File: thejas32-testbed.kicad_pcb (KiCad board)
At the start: 4 copper layers, 141.5 x 110 mm, 102 parts, among them J1 Conn_02x04_Odd_Even, J10 Conn_02x10_Odd_Even, J11 Conn_02x03_Odd_Even, J12 Conn_02x20_Odd_Even, J13 Conn_02x06_Odd_Even, J2 USB_B_Micro, J3 Conn_02x03_Odd_Even, J4 Conn_02x04_Odd_Even, J6 Conn_02x06_Odd_Even, J7 Conn_01x06, U1 Pico Master, U2 THEJAS32, U3 Pico Slave, U6 W25Q16JVSSIQ

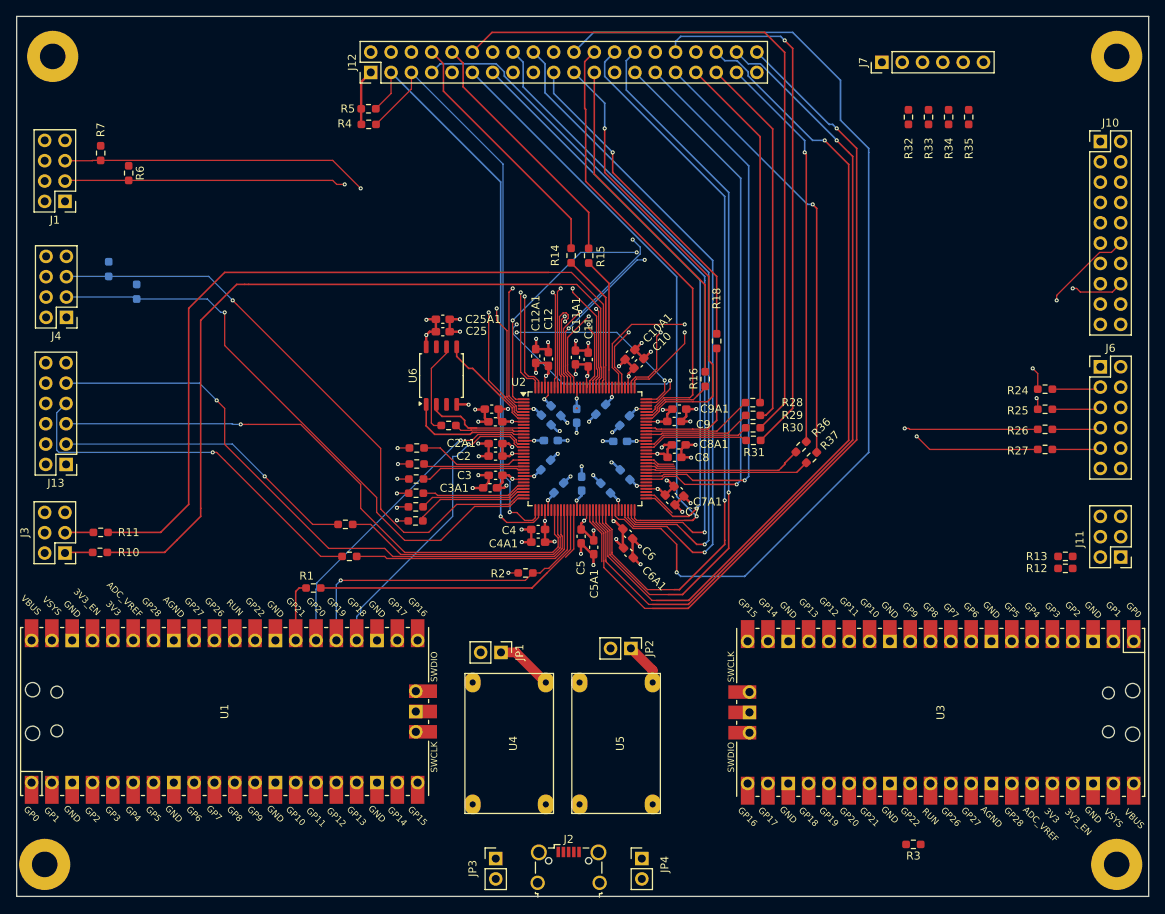
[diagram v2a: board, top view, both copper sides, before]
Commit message: Review,power shapes,dcap placement from Atharva
All dcaps are now at layer 4, leaving lot
more space on layer 1 for signal breakout.

Flow of 1V2 power is deemed good - power plane,
flowing to caps, through via to pins. Flow of 3V3
power is reasonable - power plane with vias to both
caps and pins.

Connectors and component placements need to be
finalized next, and routed.
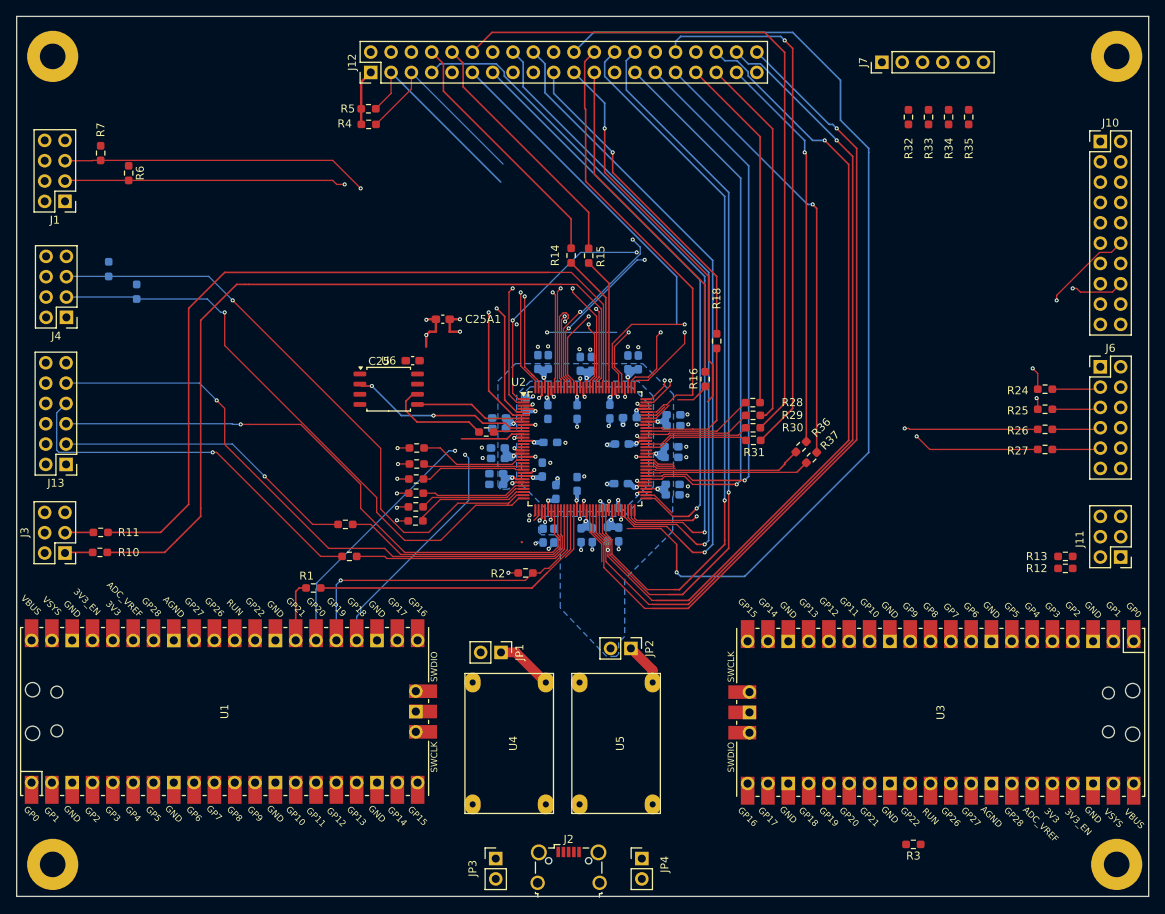
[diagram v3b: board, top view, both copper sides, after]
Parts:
- C1, C10, C10A1, C11, C11A1, C12, C12A1, C1A1, C2, C2A1, C3, C3A1, C4, C4A1, C5, C5A1, C6, C6A1, C7, C7A1, C8, C8A1, C9, C9A1: moved to B.Cu
- moved U6 6.81 mm to (131.0, 96.6), turned to 0 degrees
- moved C25 5.22 mm to (134.0, 93.0), turned to 180 degrees
- moved R70 4.78 mm to (143.2, 102.0)
- moved C13 3.13 mm to (148.2, 98.5), turned to 90 degrees
- moved C6A1 2.60 mm to (159.8, 114.8), turned to -90 degrees
- moved C1A1 2.58 mm to (144.8, 101.5)
- moved C18 2.55 mm to (158.8, 111.4), turned to 180 degrees
- moved C6 2.53 mm to (158.3, 114.7), turned to -90 degrees
- moved C5A1 2.19 mm to (155.1, 114.8)
- moved C4A1 2.12 mm to (151.7, 114.9), turned to -90 degrees
- moved C2A1 1.88 mm to (144.7, 105.2)
- moved C12A1 1.74 mm to (150.9, 93.2)
- moved C10A1 1.44 mm to (162.2, 93.2), turned to 90 degrees
- moved C5 1.40 mm to (156.4, 114.8)
- moved C10 1.38 mm to (160.9, 93.2), turned to 90 degrees
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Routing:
- net RPi_COMPAT_I2C1_SCL: track 73.2 -> 25.4 mm
- net RPi_COMPAT_I2C1_SDA: track 72.7 -> 26.2 mm
- net RPi_COMPAT_GPIO_17: track 76.2 -> 51.2 mm
- net Net-(J1-Pin_5): track 93.7 -> 69.7 mm
- net PWR_3V3: track 65.0 -> 41.1 mm
- net GND: track 83.1 -> 60.1 mm, vias 46 -> 65
- net PWR_1V2: track 81.6 -> 60.9 mm, vias 24 -> 12
- net Net-(J1-Pin_3): track 91.2 -> 80.5 mm
- net MCU_BOOT_SEL: track 41.5 -> 31.4 mm
- net MCU_HEART_BEAT: track 38.6 -> 29.2 mm
- net Net-(U2-SPI3_MISO): track 13.8 -> 22.7 mm, vias 0 -> 2
- net Net-(U2-SPI3_SS): track 15.5 -> 8.03 mm
- net RPi_COMPAT_SPI0_MISO: track 57.3 -> 52.2 mm
- net Net-(U2-SPI3_SCLK): track 8.80 -> 3.80 mm
- net RPi_COMPAT_GPIO_25: track 128.8 -> 125.9 mm
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- added copper zone on B.Cu, net GND
- added copper zone on In1.Cu, net GND
- added copper zone on B.Cu, net PWR_1V2
- removed copper zone on In2.Cu, net PWR_1V2

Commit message: Remap pins for less criss cross. Get rid of tracks
Got rid of tracks to start tracks afresh once placement is
done.
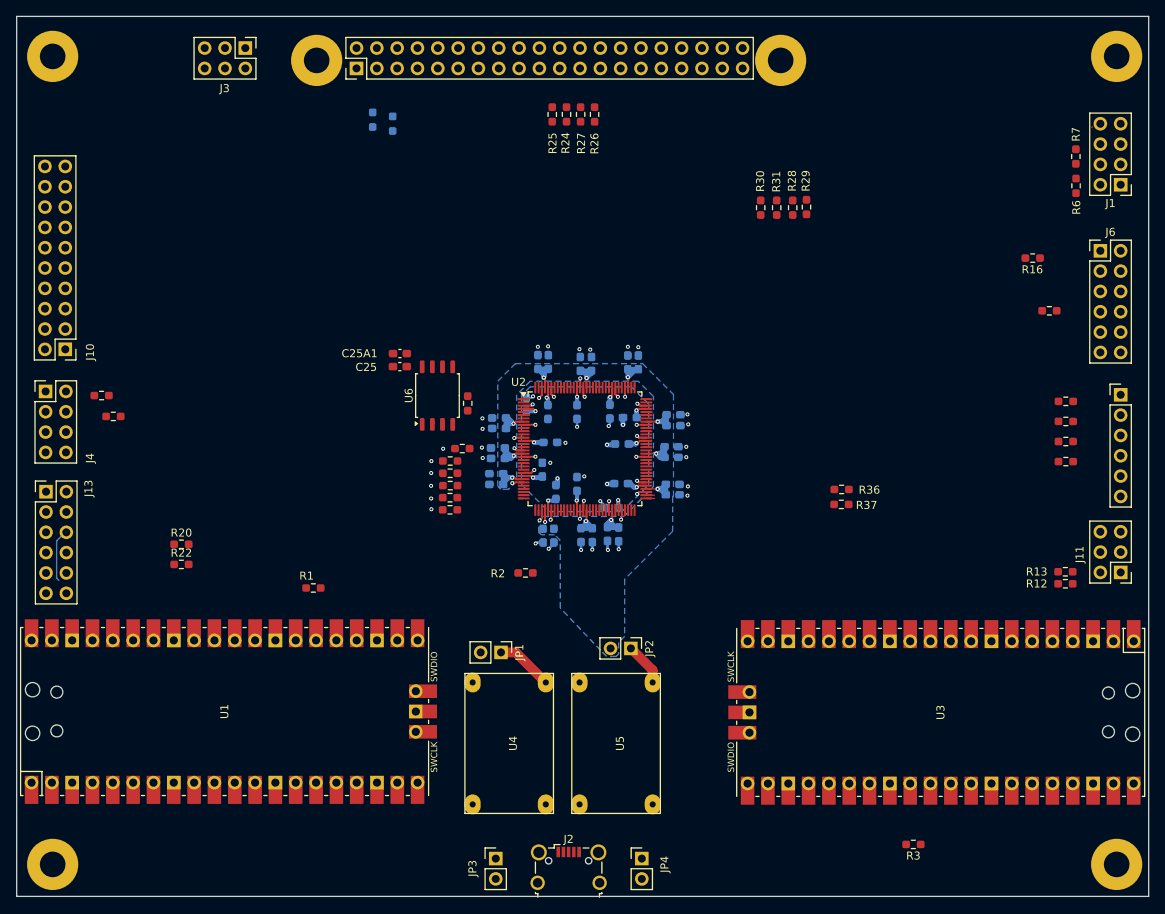
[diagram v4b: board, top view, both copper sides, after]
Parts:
- removed R10, R11, R14, R15: 0E, project_lib:proj_R_0603_1608Metric_Pad0.98x0.95mm_HandSolder
- added TP5: Mounting Hole, MountingHole:MountingHole_3.2mm_M3_Pad, F.Cu at (122.0, 55.5)
- added TP6: Mounting Hole, MountingHole:MountingHole_3.2mm_M3_Pad, F.Cu at (180.0, 55.5)
- moved J1 132.0 mm to (222.5, 71.0)
- moved J10 132.0 mm to (90.6, 91.6), turned to 180 degrees
- moved R7 121.9 mm to (216.9, 67.5), turned to 90 degrees
- moved R6 118.4 mm to (216.9, 71.2), turned to 90 degrees
- moved R25 71.8 mm to (151.4, 62.3), turned to 90 degrees
- moved R27 71.6 mm to (155.0, 62.3), turned to 90 degrees
- moved R24 69.0 mm to (153.2, 62.3), turned to 90 degrees
- moved R26 68.7 mm to (156.7, 62.3), turned to 90 degrees
- moved J3 67.0 mm to (113.1, 54.0), turned to -90 degrees
- moved J7 51.2 mm to (222.5, 97.3), turned to 0 degrees
- moved R5 50.0 mm to (96.6, 100.0), turned to 180 degrees
- moved R4 47.6 mm to (95.1, 97.4), turned to 180 degrees
- moved R35 44.7 mm to (215.6, 105.7), turned to 0 degrees
- moved R16 43.6 mm to (211.5, 80.2), turned to 180 degrees
- moved R34 43.1 mm to (215.6, 103.1), turned to 0 degrees
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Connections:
- net MCU_SPI2_CSN renamed MCU_SPI0_CSN
- net MCU_SPI2_MISO renamed MCU_SPI0_MISO
- net MCU_SPI2_MOSI renamed MCU_SPI0_MOSI
- net MCU_SPI2_SCK renamed MCU_SPI0_SCK
- J10 pad 10: MCU_GPIO_27 -> MCU_GPIO_22
- J10 pad 11: MCU_GPIO_20 -> MCU_GPIO_25
- J10 pad 12: MCU_GPIO_28 -> MCU_GPIO_24
- J10 pad 13: MCU_GPIO_21 -> MCU_GPIO_27
- J10 pad 14: MCU_GPIO_29 -> MCU_GPIO_26
- J10 pad 15: MCU_GPIO_22 -> MCU_GPIO_29
- J10 pad 16: MCU_GPIO_30 -> MCU_GPIO_28
- J10 pad 17: MCU_GPIO_23 -> MCU_GPIO_31
- J10 pad 18: MCU_GPIO_31 -> MCU_GPIO_30
- J10 pad 3: MCU_GPIO_16 -> MCU_GPIO_17
- J10 pad 4: MCU_GPIO_24 -> MCU_GPIO_16
- J10 pad 5: MCU_GPIO_17 -> MCU_GPIO_19
- J10 pad 6: MCU_GPIO_25 -> MCU_GPIO_18
- J10 pad 7: MCU_GPIO_18 -> MCU_GPIO_21
- J10 pad 8: MCU_GPIO_26 -> MCU_GPIO_20
- J10 pad 9: MCU_GPIO_19 -> MCU_GPIO_23
- J4 pad 4: MCU_I2C2_SCL -> MCU_I2C0_SCL
- J4 pad 6: MCU_I2C2_SDA -> MCU_I2C0_SCL
- R16 pad 2: RPi_COMPAT_SPI0_SCLK -> Net-(J6-Pin_3)
- R18 pad 2: RPi_COMPAT_SPI0_MOSI -> Net-(J6-Pin_7)
- R24 pad 2: Net-(J6-Pin_3) -> RPi_COMPAT_SPI0_SCLK
- R25 pad 2: Net-(J6-Pin_5) -> RPi_COMPAT_SPI0_CE0
- R26 pad 2: Net-(J6-Pin_7) -> RPi_COMPAT_SPI0_MOSI
- R27 pad 2: Net-(J6-Pin_9) -> RPi_COMPAT_SPI0_MISO
- R36 pad 2: RPi_COMPAT_GPIO_26 -> RPi_COMPAT_GPIO_4
- R37 pad 2: RPi_COMPAT_GPIO_6 -> RPi_COMPAT_GPIO_17
- R4 pad 2: RPi_COMPAT_I2C1_SCL -> Net-(J4-Pin_3)
- R5 pad 2: RPi_COMPAT_I2C1_SDA -> Net-(J4-Pin_5)
- R8 pad 2: Net-(J4-Pin_3) -> RPi_COMPAT_I2C1_SCL
- R9 pad 2: Net-(J4-Pin_5) -> RPi_COMPAT_I2C1_SDA
- U1 pad 10: MCU_I2C1_SDA -> MCU_I2C0_SCL
- U1 pad 9: MCU_I2C1_SCL -> MCU_I2C0_SCL
- U2 pad 105: Net-(U2-UART2_RX) -> RPi_COMPAT_UART_RXD
- U2 pad 106: Net-(U2-UART2_TX) -> RPi_COMPAT_UART_TXD
- U2 pad 107: Net-(U2-UART0_RX) -> Net-(J3-Pin_3)
- U2 pad 108: Net-(U2-UART0_TX) -> Net-(J3-Pin_1)
- U2 pad 31: Net-(J4-Pin_5) -> RPi_COMPAT_I2C1_SDA
- U2 pad 32: Net-(J4-Pin_3) -> RPi_COMPAT_I2C1_SCL
- U2 pad 33: RPi_COMPAT_I2C1_SCL -> Net-(J4-Pin_3)
- U2 pad 34: RPi_COMPAT_I2C1_SDA -> Net-(J4-Pin_5)
- U2 pad 53: RPi_COMPAT_GPIO_16 -> RPi_COMPAT_GPIO_26
- U2 pad 54: RPi_COMPAT_GPIO_1 -> RPi_COMPAT_GPIO_16
- U2 pad 55: RPi_COMPAT_GPIO_7 -> RPi_COMPAT_GPIO_6
- U2 pad 58: RPi_COMPAT_GPIO_25 -> RPi_COMPAT_GPIO_5
- U2 pad 61: RPi_COMPAT_GPIO_24 -> RPi_COMPAT_GPIO_0
- U2 pad 62: RPi_COMPAT_GPIO_23 -> RPi_COMPAT_GPIO_1
- U2 pad 63: RPi_COMPAT_GPIO_4 -> RPi_COMPAT_GPIO_7
- U2 pad 64: RPi_COMPAT_GPIO_17 -> RPi_COMPAT_GPIO_25
- U2 pad 65: RPi_COMPAT_GPIO_27 -> RPi_COMPAT_GPIO_24
- U2 pad 71: RPi_COMPAT_GPIO_0 -> RPi_COMPAT_GPIO_23
- U2 pad 72: RPi_COMPAT_GPIO_5 -> RPi_COMPAT_GPIO_27
- U2 pad 90: RPi_COMPAT_SPI0_MISO -> Net-(J6-Pin_9)
- U2 pad 92: RPi_COMPAT_SPI0_CE0 -> Net-(J6-Pin_5)
- U3 pad 10: MCU_I2C2_SDA -> MCU_I2C1_SDA
- U3 pad 9: MCU_I2C2_SCL -> MCU_I2C1_SCL
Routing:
- net RPi_COMPAT_GPIO_25: track 125.9 -> 0.00 mm, vias 1 -> 0
- net MCU_GPIO_24: track 109.6 -> 0.00 mm, vias 1 -> 0
- net RPi_COMPAT_GPIO_21: track 104.1 -> 0.00 mm, vias 1 -> 0
- net RPi_COMPAT_GPIO_16: track 104.0 -> 0.00 mm, vias 1 -> 0
- net RPi_COMPAT_GPIO_20: track 103.9 -> 0.00 mm, vias 1 -> 0
- net Net-(U2-UART0_RX): track 101.8 -> 0.00 mm
- net Net-(U2-UART0_TX): track 101.2 -> 0.00 mm
- net MCU_GPIO_16: track 100.9 -> 0.00 mm, vias 1 -> 0
- net MCU_GPIO_25: track 100.0 -> 0.00 mm, vias 1 -> 0
- net MCU_GPIO_17: track 97.9 -> 0.00 mm, vias 1 -> 0
- net MCU_GPIO_18: track 94.3 -> 0.00 mm, vias 1 -> 0
- net RPi_COMPAT_GPIO_1: track 93.1 -> 0.00 mm, vias 1 -> 0
- net MCU_GPIO_21: track 92.7 -> 0.00 mm, vias 1 -> 0
- net RPi_COMPAT_GPIO_7: track 92.4 -> 0.00 mm, vias 1 -> 0
- net MCU_GPIO_19: track 92.5 -> 0.62 mm, vias 2 -> 0
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
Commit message: Potentially cleaner routing
Main changes:

- No more than 1 via on high speed trace (e.g. SPI)
- Use two vias on slower GPIOs to maintain topology
- Use via on the thick 5V trace supplying power to
  RPi connector
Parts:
- removed R12, R13: 0E, project_lib:proj_R_0603_1608Metric_Pad0.98x0.95mm_HandSolder
- J7: value Conn_01x06 -> Conn_01x05; footprint Connector_PinHeader_2.54mm:PinHeader_1x06_P2.54mm_Vertical -> Connector_PinHeader_2.54mm:PinHeader_1x05_P2.54mm_Vertical
- R16, R18, R32, R33, R34, R35, R36, R37, R6, R7: moved to B.Cu
- R8: moved to F.Cu
- moved R35 43.4 mm to (175.0, 121.0)
- moved R28 20.6 mm to (161.1, 76.2)
- moved R29 20.5 mm to (162.9, 76.2)
- moved R31 13.2 mm to (166.5, 76.3)
- moved R30 13.0 mm to (164.7, 76.3)
- moved J6 13.0 mm to (222.5, 92.0), turned to 180 degrees
- moved R24 12.5 mm to (153.0, 74.8)
- moved R27 12.5 mm to (155.0, 74.8)
- moved R25 12.3 mm to (151.0, 74.6)
- moved R26 12.3 mm to (157.0, 74.6)
- moved R36 9.27 mm to (180.1, 103.7)
- moved R37 9.27 mm to (180.1, 105.6)
- moved R16 8.55 mm to (213.6, 88.5), turned to 0 degrees
- moved R20 7.57 mm to (97.6, 117.0), turned to 180 degrees
- moved R7 6.51 mm to (217.4, 74.0), turned to 0 degrees
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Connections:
- J4 pad 6: MCU_I2C0_SCL -> MCU_I2C0_SDA
- J7 pad 5: MCU_PWM_7 -> GND
- U1 pad 10: MCU_I2C0_SCL -> MCU_I2C0_SDA
- U1 pad 25: MCU_RESETN -> unconnected-(U1-GPIO19-Pad25)
- U2 pad 45: Net-(U2-UART1_TX) -> Net-(J11-Pin_1)
- U2 pad 50: Net-(U2-UART1_RX) -> Net-(J11-Pin_3)
- U2 pad 61: RPi_COMPAT_GPIO_0 -> RPi_COMPAT_GPIO_1
- U2 pad 62: RPi_COMPAT_GPIO_1 -> RPi_COMPAT_GPIO_0
- U2 pad 66: RPi_COMPAT_GPIO_22 -> RPi_COMPAT_GPIO_23
- U2 pad 71: RPi_COMPAT_GPIO_23 -> RPi_COMPAT_GPIO_22
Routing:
- net PWR_3V3: track 28.4 -> 467.2 mm, vias 12 -> 15
- net PICO_SLAVE_RUN: track 0.00 -> 136.8 mm
- net PICO_COMM_1: track 0.00 -> 99.4 mm
- net MCU_BOOT_UART_RX: track 0.00 -> 94.6 mm, vias 0 -> 1
- net MCU_BOOT_UART_TX: track 0.00 -> 94.0 mm, vias 0 -> 1
- net RPi_COMPAT_GPIO_21: track 0.00 -> 92.7 mm
- net RPi_COMPAT_GPIO_25: track 0.00 -> 92.3 mm, vias 0 -> 2
- net RPi_COMPAT_GPIO_23: track 0.00 -> 92.3 mm, vias 0 -> 2
- net RPi_COMPAT_GPIO_20: track 0.00 -> 92.2 mm
- net RPi_COMPAT_GPIO_1: track 0.00 -> 92.2 mm, vias 0 -> 2
- net RPi_COMPAT_GPIO_24: track 1.06 -> 92.2 mm, vias 0 -> 1
- net RPi_COMPAT_GPIO_16: track 0.00 -> 90.3 mm, vias 0 -> 1
- net RPi_COMPAT_GPIO_7: track 0.00 -> 90.0 mm, vias 0 -> 2
- net RPi_COMPAT_GPIO_6: track 0.00 -> 89.9 mm, vias 0 -> 1
- net RPi_COMPAT_GPIO_5: track 0.00 -> 89.7 mm, vias 0 -> 1
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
